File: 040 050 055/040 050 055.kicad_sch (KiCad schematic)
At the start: 3 parts, among them J1 USB

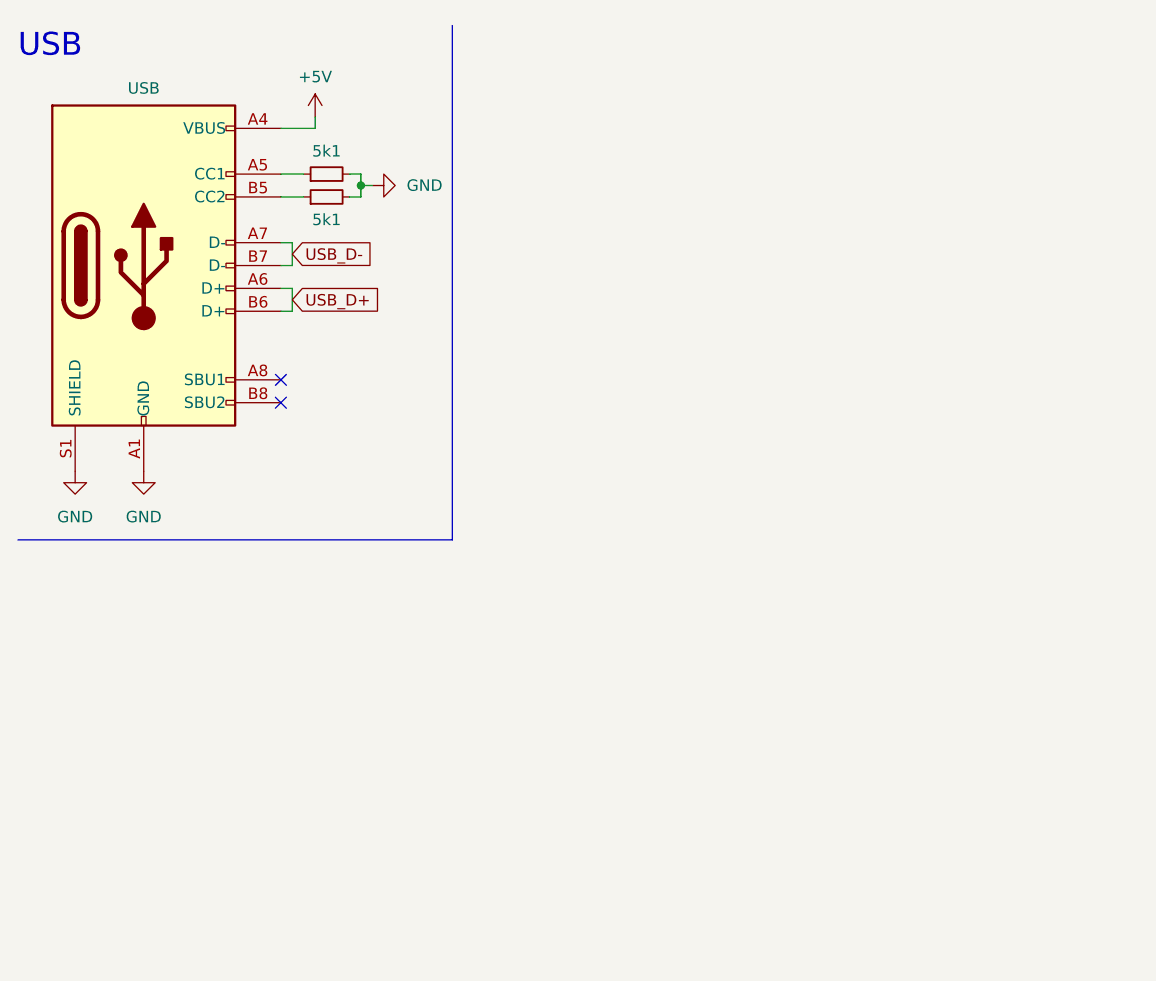
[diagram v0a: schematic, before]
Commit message: Feature Complete Schema. Begin footprint creation
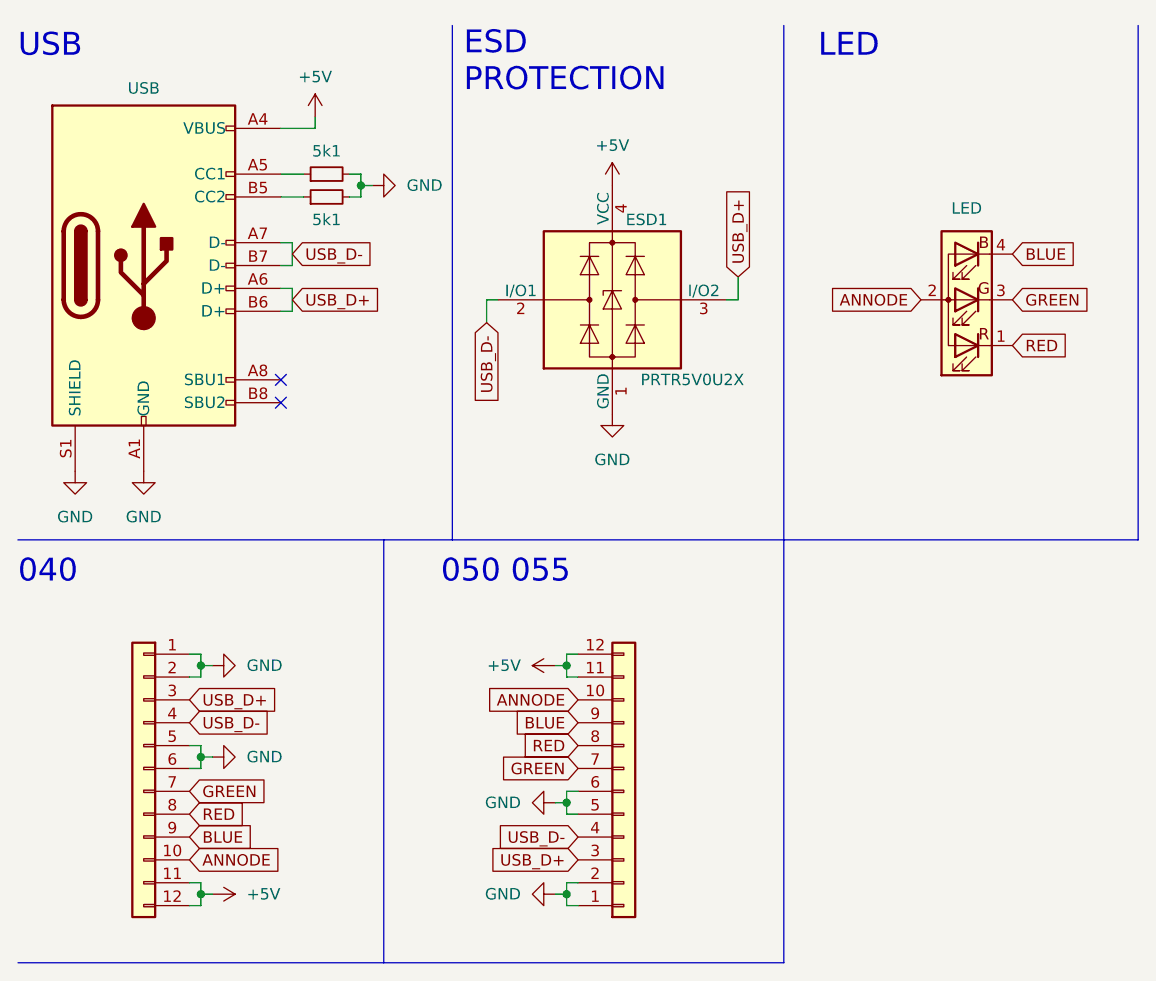
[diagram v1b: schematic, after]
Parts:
- added ESD1: PRTR5V0U2X, Package_TO_SOT_SMD:SOT-143, symbol Power_Protection:PRTR5V0U2X
- added J05x1: 05x, symbol Connector_Generic:Conn_01x12
- added J40: 040, symbol Connector_Generic:Conn_01x12
- added LED1: LED, symbol Device:LED_RAGB
- R1, R2: footprint (none) -> Resistor_SMD:R_0603_1608Metric
- renumbered J1 to JUSB1
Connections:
- net +5V: now also ESD1.4 (VCC), J05x1.11 (Pin_11), J05x1.12 (Pin_12), J40.11 (Pin_11), J40.12 (Pin_12)
- net GND: now also ESD1.1 (GND), J05x1.1 (Pin_1), J05x1.2 (Pin_2), J05x1.5 (Pin_5), J05x1.6 (Pin_6), J40.1 (Pin_1), J40.2 (Pin_2), J40.5 (Pin_5), J40.6 (Pin_6)
- net USB_D+: now also ESD1.3 (I/O2), J05x1.3 (Pin_3), J40.3 (Pin_3)
- net USB_D-: now also ESD1.2 (I/O1), J05x1.4 (Pin_4), J40.4 (Pin_4)
- new net ANNODE: J05x1.10 (Pin_10), J40.10 (Pin_10), LED1.2 (A)
- new net BLUE: J05x1.9 (Pin_9), J40.9 (Pin_9), LED1.4 (BK)
- new net GREEN: J05x1.7 (Pin_7), J40.7 (Pin_7), LED1.3 (GK)
- new net RED: J05x1.8 (Pin_8), J40.8 (Pin_8), LED1.1 (RK)
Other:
- note added: "040"
- note added: "050 055"
- note added: "ESD PROTECTION"
- note added: "LED"

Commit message: Unknown Changes
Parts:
- JUSB1: footprint (none) -> Connector_Custom:YTC-16S-28
- LED1: footprint (none) -> LED_Custom:FM-3510RGBA-SG
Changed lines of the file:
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@@
       (effects (font (size 1.27 1.27)))
     )
-    (property "Footprint" "" (at 118.11 41.91 0)
+    (property "Footprint" "LED_Custom:FM-3510RGBA-SG" (at 118.11 41.91 0)
       (effects (font (size 1.27 1.27)) hide)
     )
@@
       (effects (font (size 1.27 1.27)) hide)
     )
-    (property "Value" "USB" (at 26.67 19.685 0)
+    (property "Value" "USB" (at 26.67 19.05 0)
       (effects (font (size 1.27 1.27)))
     )
-    (property "Footprint" "" (at 30.48 39.37 0)
+    (property "Footprint" "Connector_Custom:YTC-16S-28" (at 30.48 39.37 0)
       (effects (font (size 1.27 1.27)) hide)
     )
